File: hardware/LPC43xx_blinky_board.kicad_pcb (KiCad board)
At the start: 4 copper layers, 76.2 x 49.5 mm, 66 parts, among them J1 Conn_01x04_Male, J2 Conn_ARM_JTAG_SWD_10, J3 USB_B_Micro, J4 Conn_01x20_Female, J5 Micro_SD_Card, J6 Conn_01x04_Female, J7 Conn_01x08_Female, J8 Conn_01x16_Female, SW1 SW_DIP_x01, SW2 SW_DIP_x04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

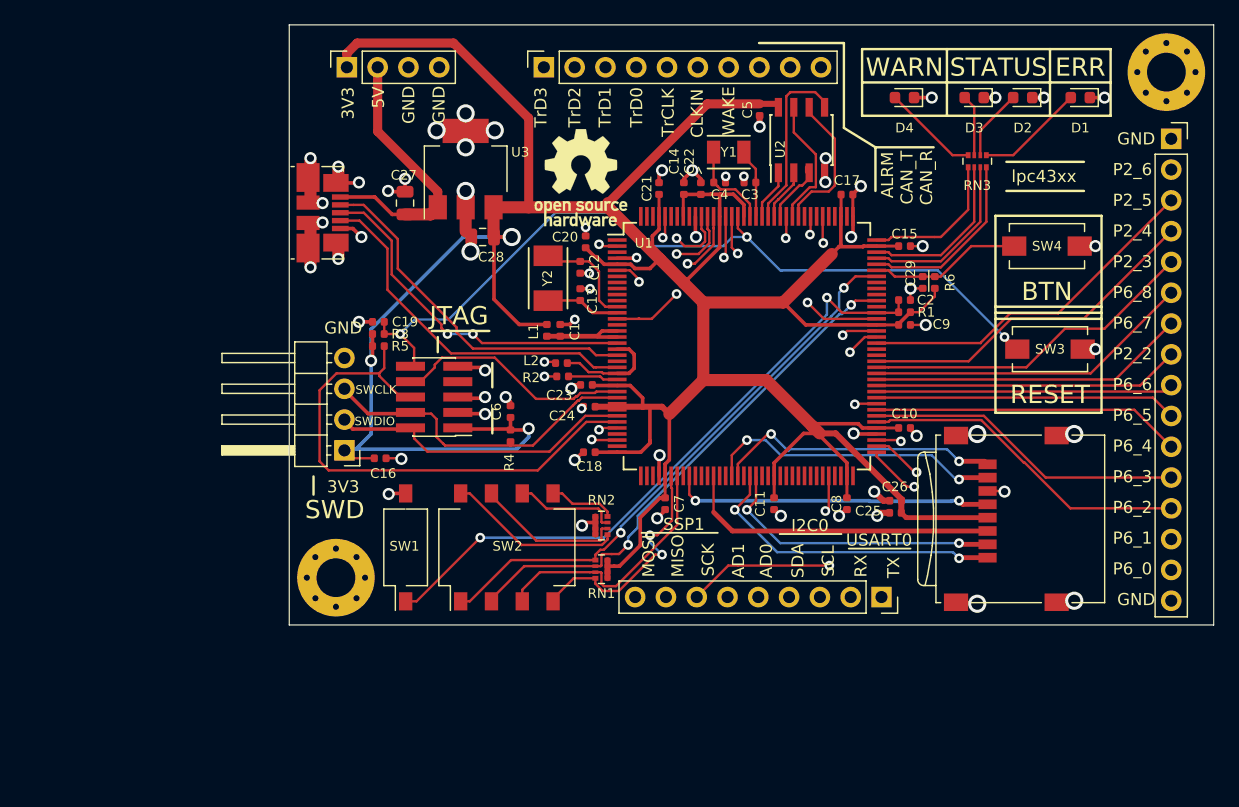
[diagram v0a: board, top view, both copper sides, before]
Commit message: Fix grid and move two caps out of sd card area
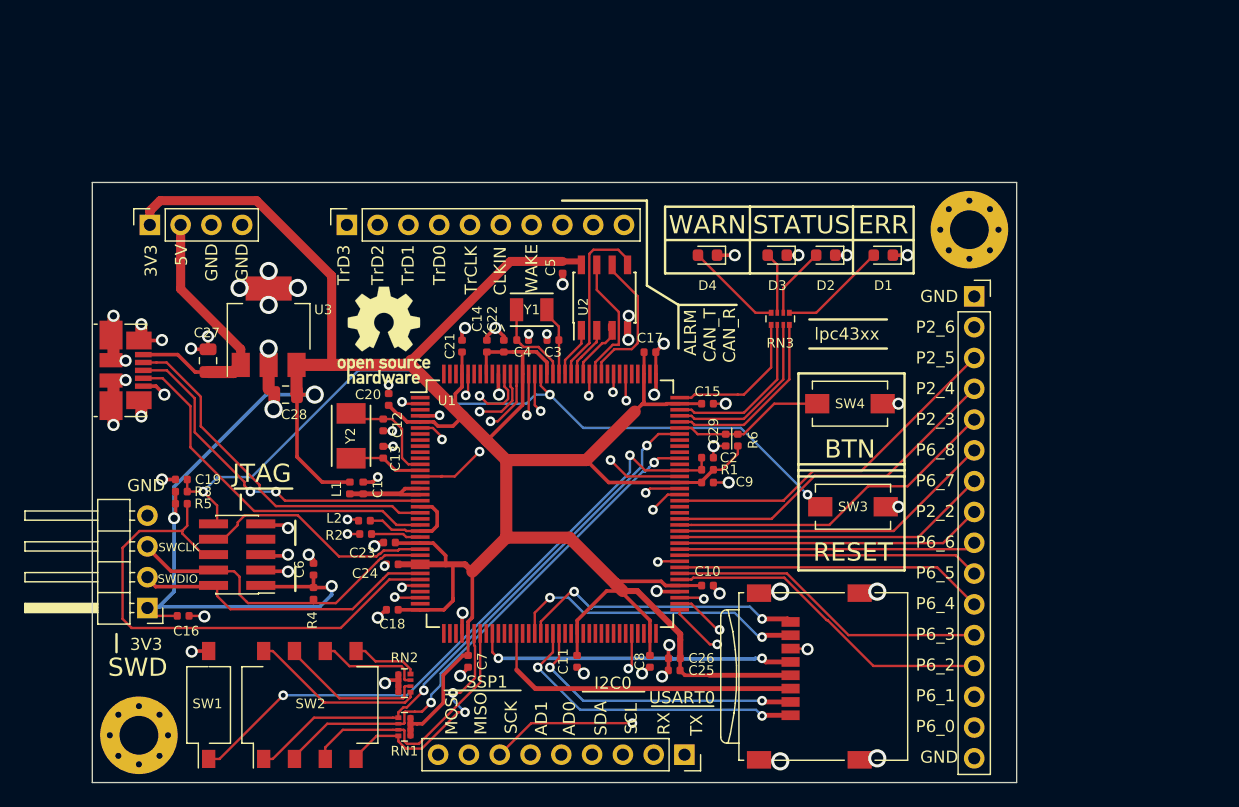
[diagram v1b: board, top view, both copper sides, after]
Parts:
- moved C25 22.4 mm to (143.0, 115.8)
- moved C26 22.4 mm to (143.0, 114.8)
- moved C14 20.8 mm to (127.5, 89.0)
- moved R2 20.8 mm to (117.5, 104.5)
- moved REF** 20.8 mm to (119.0, 88.1)
- moved C1 20.8 mm to (117.3, 100.7)
- moved C10 20.8 mm to (145.8, 108.8)
- moved C11 20.8 mm to (135.0, 115.0)
- moved C12 20.8 mm to (119.0, 95.5)
- moved C13 20.8 mm to (119.0, 97.8)
- moved C15 20.8 mm to (145.8, 93.8)
- moved C16 20.8 mm to (102.5, 111.2)
- moved C17 20.8 mm to (141.0, 89.5)
- moved C18 20.8 mm to (119.8, 110.8)
- moved C19 20.8 mm to (102.3, 100.0)
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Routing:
- net +3V3: track 295.8 -> 296.9 mm

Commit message: PCB design: small adjustments according to pre-order checklist
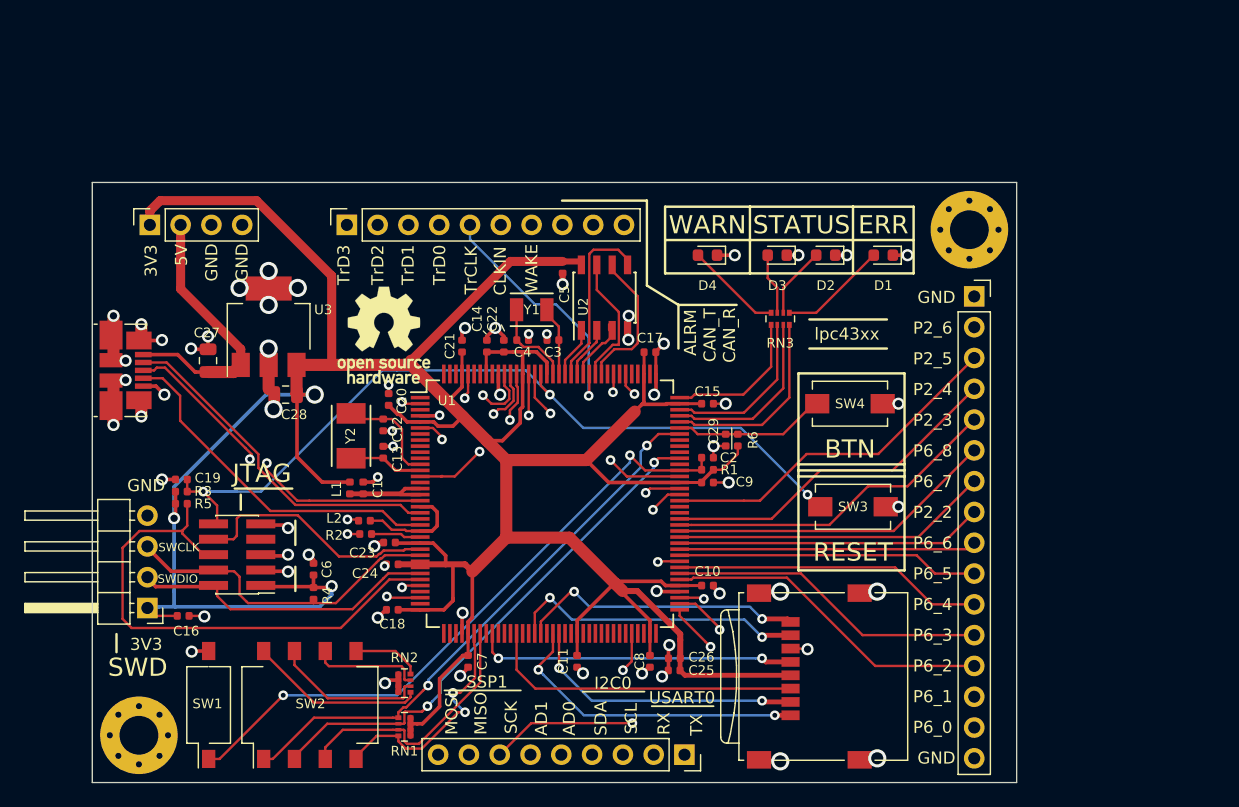
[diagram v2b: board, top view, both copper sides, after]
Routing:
- net /WAKUP: track 26.5 -> 19.7 mm
- net /CLKIN: track 33.2 -> 27.0 mm
- net /ALARM: track 24.6 -> 20.9 mm
- net /~RESET: track 67.9 -> 70.1 mm
- net /TRACECLK: track 22.8 -> 21.0 mm
- net /TRACEDATA0: track 24.3 -> 22.6 mm
- net /P6_0: track 28.5 -> 30.0 mm
- net /TRACEDATA3: track 21.0 -> 22.3 mm
- net /SD_DAT3: track 24.4 -> 23.4 mm
- net /USB_HS_D-: track 29.4 -> 28.4 mm
- net /SSP1_MOSI: track 16.6 -> 17.6 mm
- net /LED_RED: track 15.2 -> 16.1 mm
- net +3V3: track 296.9 -> 296.1 mm
- net /USB_ID: track 29.6 -> 28.9 mm
- net /TRACEDATA1: track 23.7 -> 22.9 mm
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
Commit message: Hardware: adjust pcb desigh according to checklist
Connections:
- MH1 pad 1: Net-(MH1-Pad1) -> GND
- MH2 pad 1: Net-(MH2-Pad1) -> GND

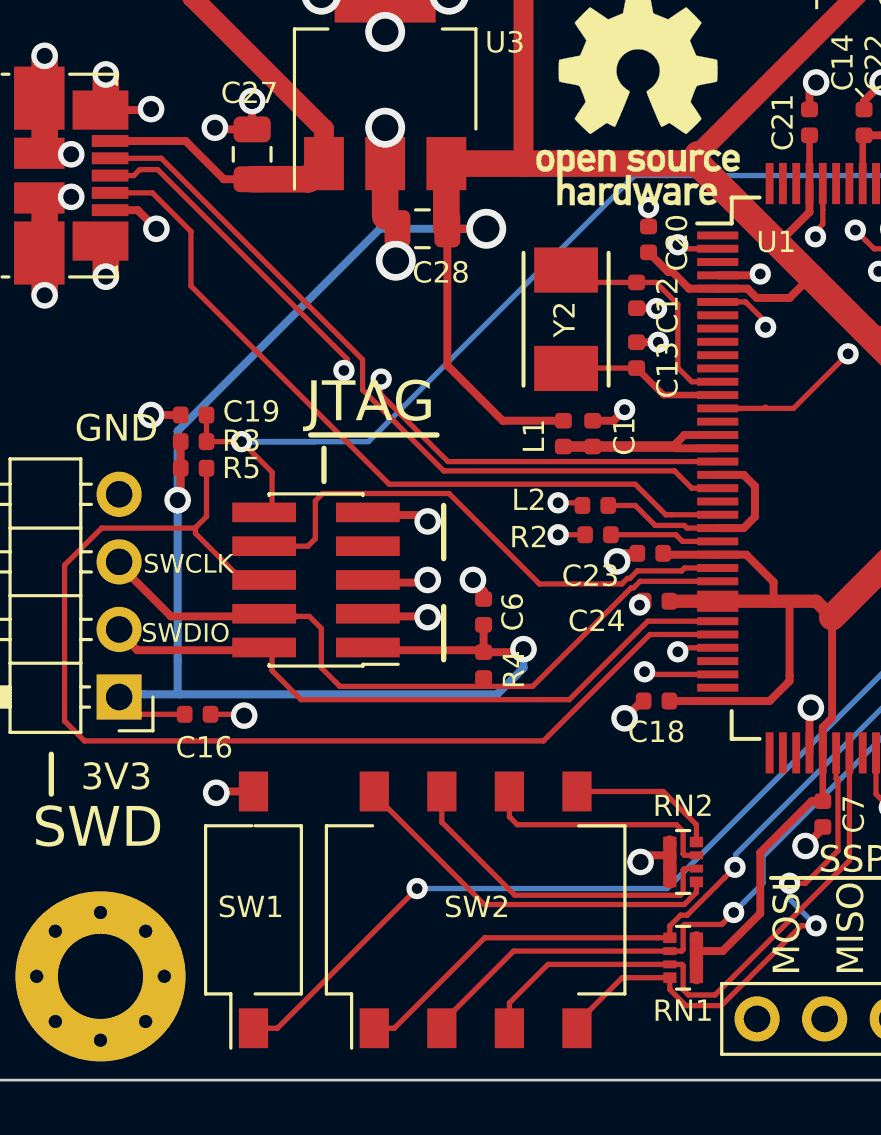
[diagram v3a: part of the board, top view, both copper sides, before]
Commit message: Update pcb: connect usb_vbus
USB_VBUS is needed for USB BOOT ROM.
ISP switch capacitor decreased to 2.2nF. 100nF was to high/slow for
power up to ISP mode
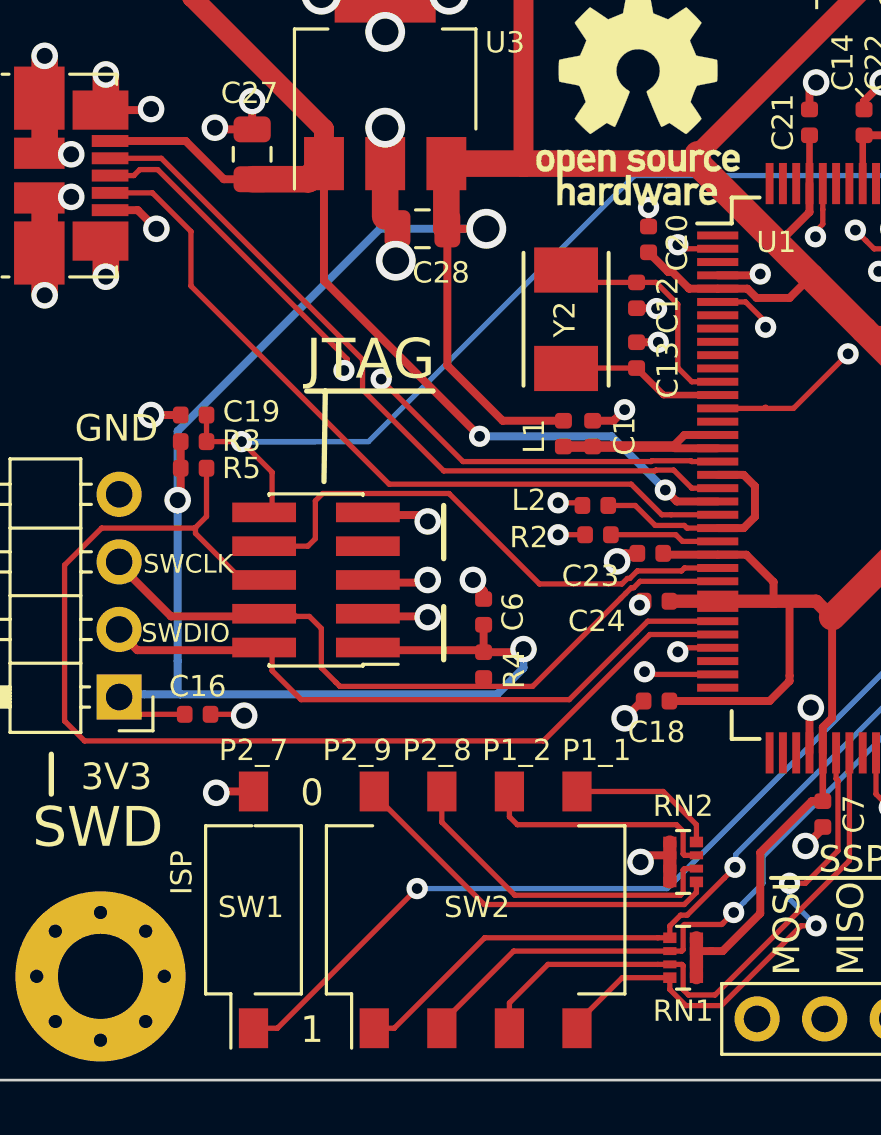
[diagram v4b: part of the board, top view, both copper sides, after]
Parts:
- C2: value 100nF -> 2.2nF
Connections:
- J2 pad 7: Net-(J2-Pad7) -> (no net)
- RN3 pad 6: /LED_GREEN -> /LED_BLUE
- RN3 pad 7: /LED_BLUE -> /LED_GREEN
- U1 pad 1: Net-(U1-Pad1) -> (no net)
- U1 pad 10: Net-(U1-Pad10) -> (no net)
- U1 pad 100: Net-(U1-Pad100) -> (no net)
- U1 pad 101: Net-(U1-Pad101) -> (no net)
- U1 pad 11: Net-(U1-Pad11) -> (no net)
- U1 pad 110: Net-(U1-Pad110) -> (no net)
- U1 pad 112: Net-(U1-Pad112) -> (no net)
- U1 pad 113: Net-(U1-Pad113) -> (no net)
- U1 pad 115: Net-(U1-Pad115) -> (no net)
- U1 pad 117: Net-(U1-Pad117) -> (no net)
- U1 pad 136: Net-(U1-Pad136) -> (no net)
- U1 pad 138: Net-(U1-Pad138) -> (no net)
- U1 pad 139: Net-(U1-Pad139) -> (no net)
- U1 pad 142: Net-(U1-Pad142) -> (no net)
- U1 pad 143: Net-(U1-Pad143) -> (no net)
- U1 pad 144: Net-(U1-Pad144) -> (no net)
- U1 pad 15: Net-(U1-Pad15) -> (no net)
- U1 pad 21: Net-(U1-Pad21) -> VBUS
- U1 pad 3: Net-(U1-Pad3) -> (no net)
- U1 pad 33: Net-(U1-Pad33) -> (no net)
- U1 pad 35: Net-(U1-Pad35) -> (no net)
- U1 pad 37: Net-(U1-Pad37) -> (no net)
- U1 pad 38: Net-(U1-Pad38) -> (no net)
- U1 pad 39: Net-(U1-Pad39) -> (no net)
- U1 pad 44: Net-(U1-Pad44) -> (no net)
- U1 pad 46: Net-(U1-Pad46) -> (no net)
- U1 pad 47: Net-(U1-Pad47) -> (no net)
- U1 pad 48: Net-(U1-Pad48) -> (no net)
- U1 pad 50: Net-(U1-Pad50) -> (no net)
- U1 pad 51: Net-(U1-Pad51) -> (no net)
- U1 pad 54: Net-(U1-Pad54) -> (no net)
- U1 pad 57: Net-(U1-Pad57) -> (no net)
- U1 pad 58: Net-(U1-Pad58) -> (no net)
- U1 pad 60: Net-(U1-Pad60) -> (no net)
- U1 pad 61: Net-(U1-Pad61) -> (no net)
- U1 pad 62: Net-(U1-Pad62) -> (no net)
- U1 pad 63: Net-(U1-Pad63) -> (no net)
- U1 pad 64: Net-(U1-Pad64) -> (no net)
- U1 pad 65: Net-(U1-Pad65) -> (no net)
- U1 pad 66: Net-(U1-Pad66) -> (no net)
- U1 pad 67: Net-(U1-Pad67) -> (no net)
- U1 pad 69: Net-(U1-Pad69) -> (no net)
- U1 pad 7: Net-(U1-Pad7) -> (no net)
- U1 pad 70: Net-(U1-Pad70) -> (no net)
- U1 pad 72: Net-(U1-Pad72) -> (no net)
- U1 pad 8: Net-(U1-Pad8) -> (no net)
- U1 pad 89: Net-(U1-Pad89) -> (no net)
- U1 pad 9: Net-(U1-Pad9) -> (no net)
- U1 pad 90: Net-(U1-Pad90) -> (no net)
- U1 pad 97: Net-(U1-Pad97) -> (no net)
- U1 pad 99: Net-(U1-Pad99) -> (no net)
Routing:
- net VBUS: track 22.3 -> 44.9 mm, vias 0 -> 2
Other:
- board text added: "0"
- board text added: "1"
- board text added: "ISP"
- board text added: "P1_1"
- board text added: "P1_2"
- board text added: "P2_7"
- board text added: "P2_8"
- board text added: "P2_9"
